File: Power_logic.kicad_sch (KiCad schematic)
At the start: 0 parts

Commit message: power led
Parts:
- added D8: APHHS1005LSECK/J3-PF, LED_SMD:LED_0402_1005Metric, symbol #dzdb:s_dio/D-KIN-APHHS1005LSECK/J3-PF
- added R19: 1.6k, Resistor_SMD:R_0603_1608Metric, symbol #dzdb:g_res/R-1.6k-0603
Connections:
- new net: D8.2 (A), R19.2
- new net +5V: R19.1
- new net GND: D8.1 (K)
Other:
- note added: "if there is a battery connected, the LED will light up and you should not plug in your USB cable/STM connector."

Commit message: simple changes
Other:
- note added: "Wont work... diodes are not perfect..."
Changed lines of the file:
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@@
 	(generator_version "9.0")
 	(paper "A4")
+	(text "Wont work... diodes are not perfect..."
+		(exclude_from_sim no)
+		(at 90.424 73.66 0)
+		(effects
+			(font
+				(size 1.27 1.27)
+			)
+		)
+	)
 	(text "if there is a battery connected,\nthe LED will light up and you should\nnot plug in your USB cable/STM connector."
 		(exclude_from_sim no)

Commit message: Added Power logic finally. (plus some comments on further improvements)
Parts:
- renumbered D8 to D9, R19 to R15
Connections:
- net +5V: no longer names the net of R15.1
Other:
- added sheet 3.3V_Logic (3.3V_Logic.kicad_sch)
- added sheet 5V_Logic (5V_Logic.kicad_sch)
- added sheet GPIO_REF3.3V (GPIO_REF3.3V.kicad_sch)
- note added: "Lan only if plugged in (battery)"
- note added: "Whenever the CM4 runs, also run the LED signals AND the SSD voltage. all "core" tasks tied to the CM4. If I forgot something please let me know."
- note added: "some rules: USB wont power the STM32. STM_Plug wont power the CM4 The GPIO_VREF of the CM4 needs to be STM32's 3.3V The Lan Vin is only powered when running on Battery Battery preferrably powers everything."
- moved on the sheet: D9, R15

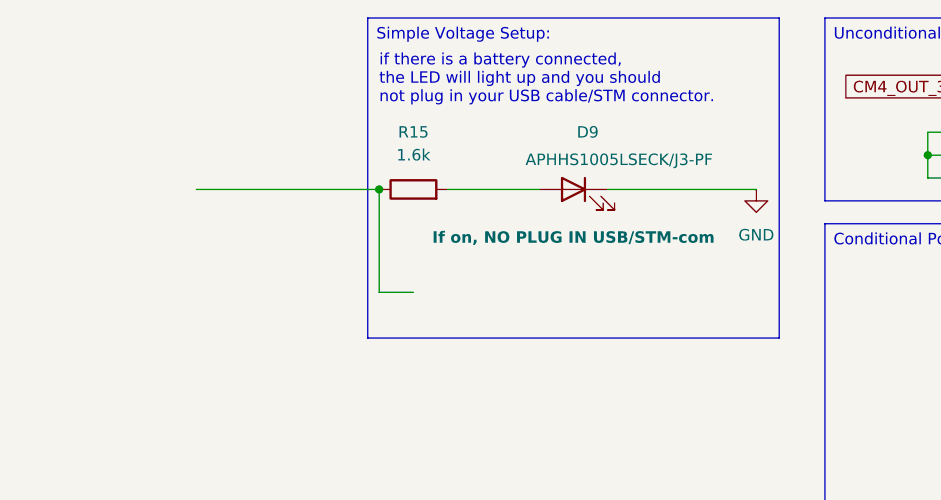
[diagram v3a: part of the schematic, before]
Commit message: tried to find some placements for power routing
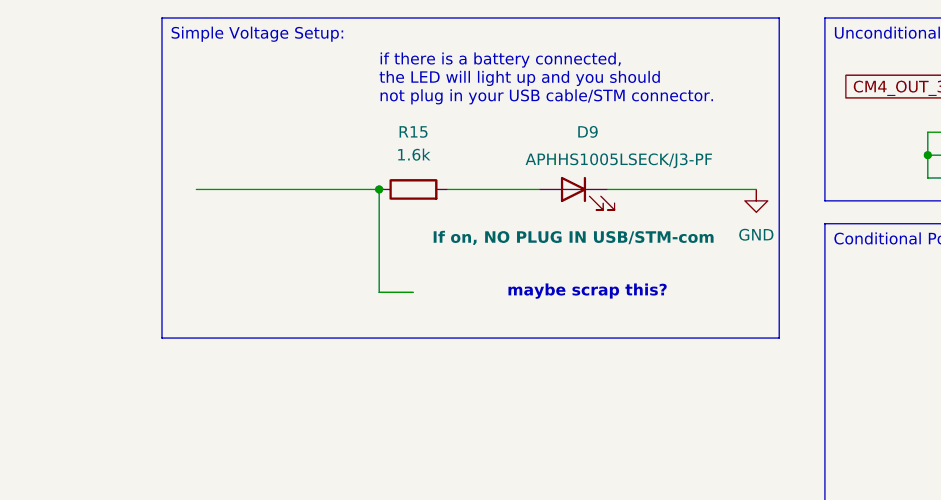
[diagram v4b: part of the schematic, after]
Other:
- note added: "maybe scrap this?"
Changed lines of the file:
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@@
+		)
+	)
+	(text "maybe scrap this?"
+		(exclude_from_sim no)
+		(at 73.914 48.26 0)
+		(effects
+			(font
+				(size 1.27 1.27)
+				(thickness 0.254)
+				(bold yes)
+				(color 255 200 84 1)
+			)
+			(justify left)
 		)
 	)
@@
 	(text_box "Simple Voltage Setup:"
 		(exclude_from_sim no)
-		(at 58.42 17.78 0)
-		(size 45.72 35.56)
+		(at 35.56 17.78 0)
+		(size 68.58 35.56)
 		(margins 0.9525 0.9525 0.9525 0.9525)
 		(stroke

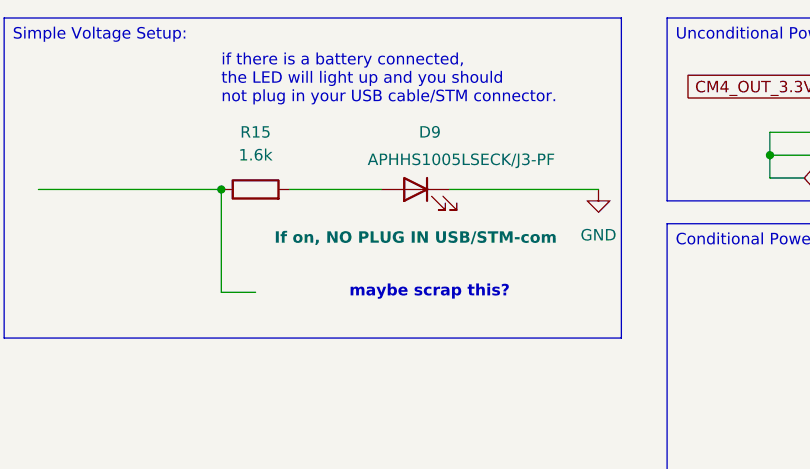
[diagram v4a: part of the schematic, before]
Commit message: multiple changes to the differential pair for easier routing later.
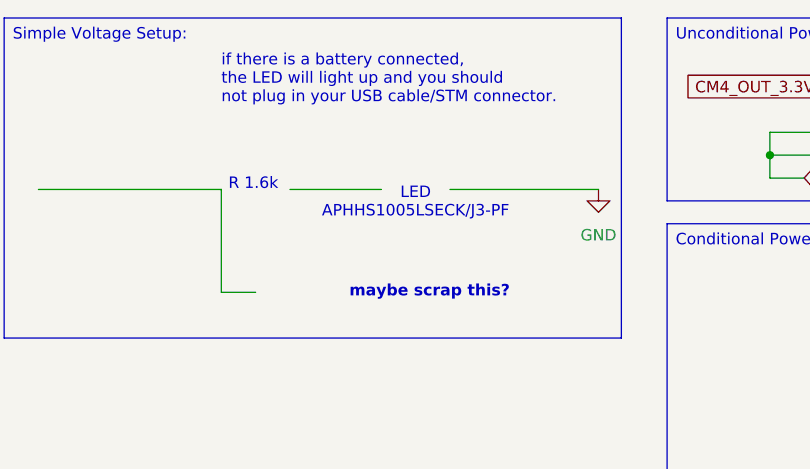
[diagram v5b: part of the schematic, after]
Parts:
- removed D9: APHHS1005LSECK/J3-PF, LED_SMD:LED_0402_1005Metric, symbol #dzdb:s_dio/D-KIN-APHHS1005LSECK/J3-PF
- removed R15: 1.6k, Resistor_SMD:R_0603_1608Metric, symbol #dzdb:g_res/R-1.6k-0603
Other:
- note added: "LED APHHS1005LSECK/J3-PF"
- note added: "R 1.6k"

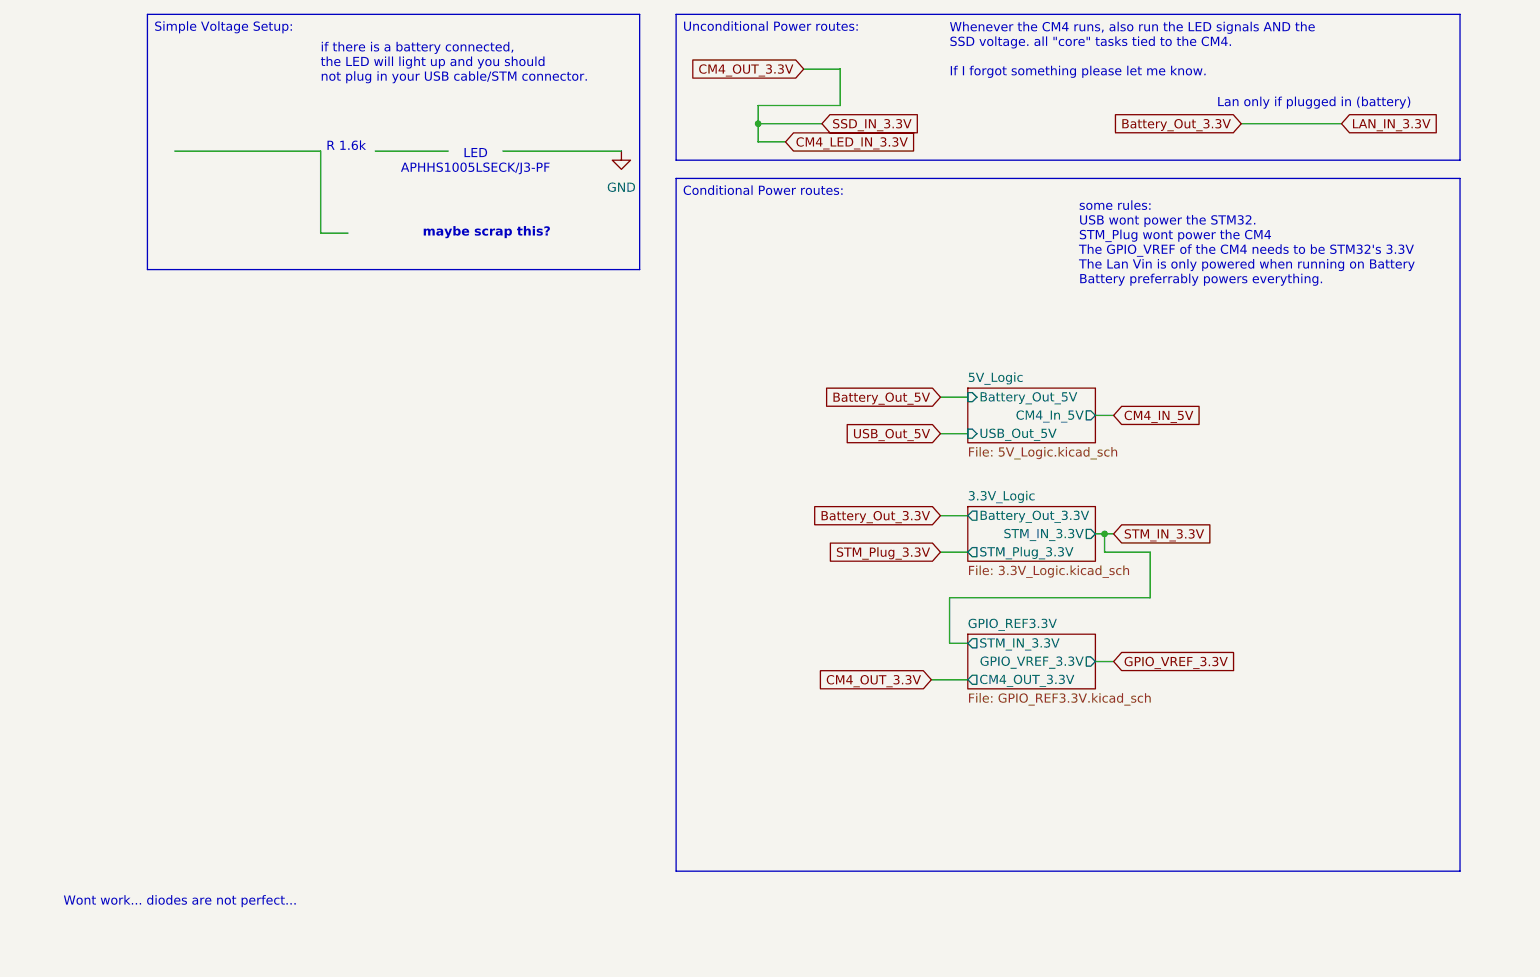
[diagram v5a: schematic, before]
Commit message: added Gyroscope and Accelerometer part (4x) over IIC
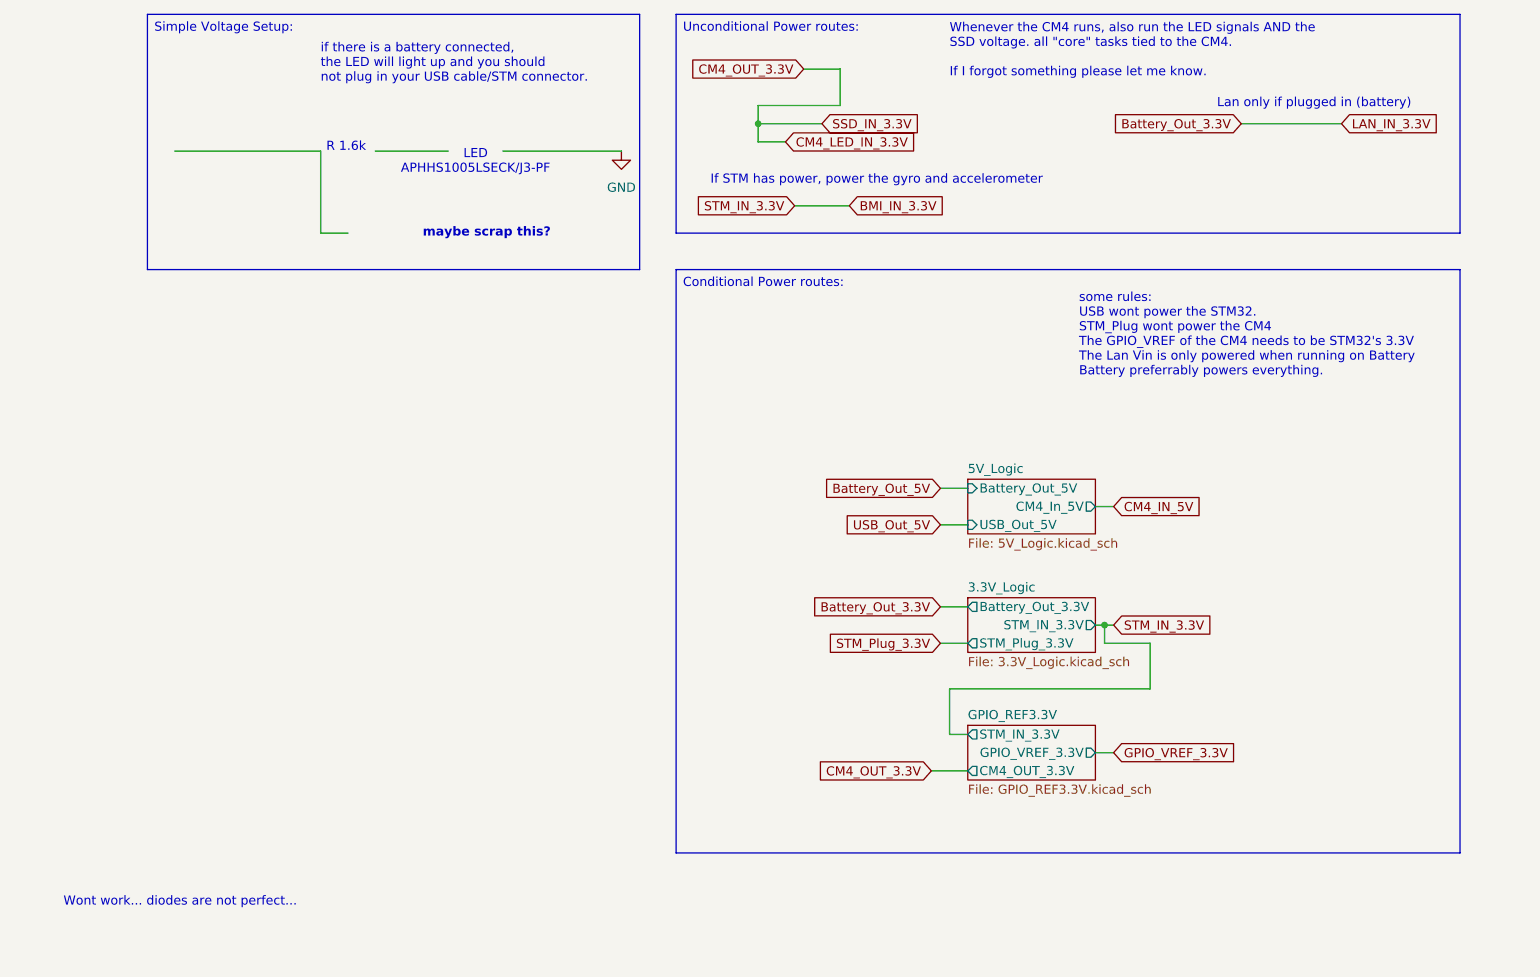
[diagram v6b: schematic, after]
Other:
- note added: "If STM has power, power the gyro and accelerometer"

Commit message: multiple chainges on PCB
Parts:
- added R32, R33, R34, R35, R36, R37: DNP, Resistor_SMD:R_0603_1608Metric, symbol #dzdb:g_res/R-0-0603
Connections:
- net BMI_IN_3.3V: now also R32.1, R34.2, R35.2
- net Battery_Out_3.3V: now also R34.1
- net Battery_Out_5V: now also R37.1
- net CM4_IN_5V: now also R36.2, R37.2
- net CM4_LED_IN_3.3V: now also R33.2
- net GPIO_VREF_3.3V: now also R32.2, R33.1
- net STM_Plug_3.3V: now also R35.1
- net USB_Out_5V: now also R36.1

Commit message: nearly complete with the PCB
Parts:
- renumbered R35 to Bat_3.3V_direct1, R36 to Bat_5V_direct1, R34 to Plug_3.3V_direct1, R37 to USB_5V_direct1, R33 to Vref_3.3V_CM41, R32 to Vref_3.3V_STM1
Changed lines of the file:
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@@
 		(on_board yes)
 		(dnp no)
-		(property "Reference" "R32"
+		(property "Reference" "Vref_3.3V_STM1"
 			(at 182.88 111.7599 0)
 			(effects
@@
 			(project ""
 				(path "/ce1819b2-f280-40ed-834f-6fe4d12f809d/c1998c4d-3f9a-4761-b447-a813532738a0"
-					(reference "R32")
+					(reference "Vref_3.3V_STM1")
 					(unit 1)
 				)
@@
 		(on_board yes)
 		(dnp no)
-		(property "Reference" "R37"
+		(property "Reference" "USB_5V_direct1"
 			(at 154.94 69.85 90)
 			(effects
@@
 			(project "nautilus_mainboard"
 				(path "/ce1819b2-f280-40ed-834f-6fe4d12f809d/c1998c4d-3f9a-4761-b447-a813532738a0"
-					(reference "R37")
+					(reference "USB_5V_direct1")
 					(unit 1)
 				)
@@
 		(on_board yes)
 		(dnp no)
-		(property "Reference" "R35"
+		(property "Reference" "Bat_3.3V_direct1"
 			(at 143.51 111.7599 0)
 			(effects
@@
 			(project "nautilus_mainboard"
 				(path "/ce1819b2-f280-40ed-834f-6fe4d12f809d/c1998c4d-3f9a-4761-b447-a813532738a0"
-					(reference "R35")
+					(reference "Bat_3.3V_direct1")
 					(unit 1)
 				)
@@
 		(on_board yes)
 		(dnp no)
-		(property "Reference" "R33"
-			(at 153.67 128.27 90)
+		(property "Reference" "Vref_3.3V_CM41"
+			(at 153.924 131.826 90)
 			(effects
 				(font
@@
 			(project "nautilus_mainboard"
 				(path "/ce1819b2-f280-40ed-834f-6fe4d12f809d/c1998c4d-3f9a-4761-b447-a813532738a0"
-					(reference "R33")
+					(reference "Vref_3.3V_CM41")
 					(unit 1)
 				)
@@
 		(on_board yes)
 		(dnp no)
-		(property "Reference" "R34"
-			(at 135.89 111.7599 0)
+		(property "Reference" "Plug_3.3V_direct1"
+			(at 131.572 118.364 0)
 			(effects
 				(font
@@
 			(project "nautilus_mainboard"
 				(path "/ce1819b2-f280-40ed-834f-6fe4d12f809d/c1998c4d-3f9a-4761-b447-a813532738a0"
-					(reference "R34")
+					(reference "Plug_3.3V_direct1")
 					(unit 1)
 				)
@@
 		(on_board yes)
 		(dnp no)
-		(property "Reference" "R36"
+		(property "Reference" "Bat_5V_direct1"
 			(at 154.94 67.31 90)
 			(effects
@@
 			(project "nautilus_mainboard"
 				(path "/ce1819b2-f280-40ed-834f-6fe4d12f809d/c1998c4d-3f9a-4761-b447-a813532738a0"
-					(reference "R36")
+					(reference "Bat_5V_direct1")
 					(unit 1)
 				)
